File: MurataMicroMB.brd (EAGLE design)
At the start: 90 x 63 mm, 59 parts, among them CON1 C-2395, CON2 WM17143CT-ND, CON3 CON_MIL_10_ARM, CON4 C-2395, IC1 NC7SZ00M5XCT-ND, IC2 296-35164-1-ND, IC3 IC_LPC11U3XQFN33, IC4 AZ1117EH-3.3TRG1DICT-ND, Q1 1253-1168-1-ND, SW1 P-8073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

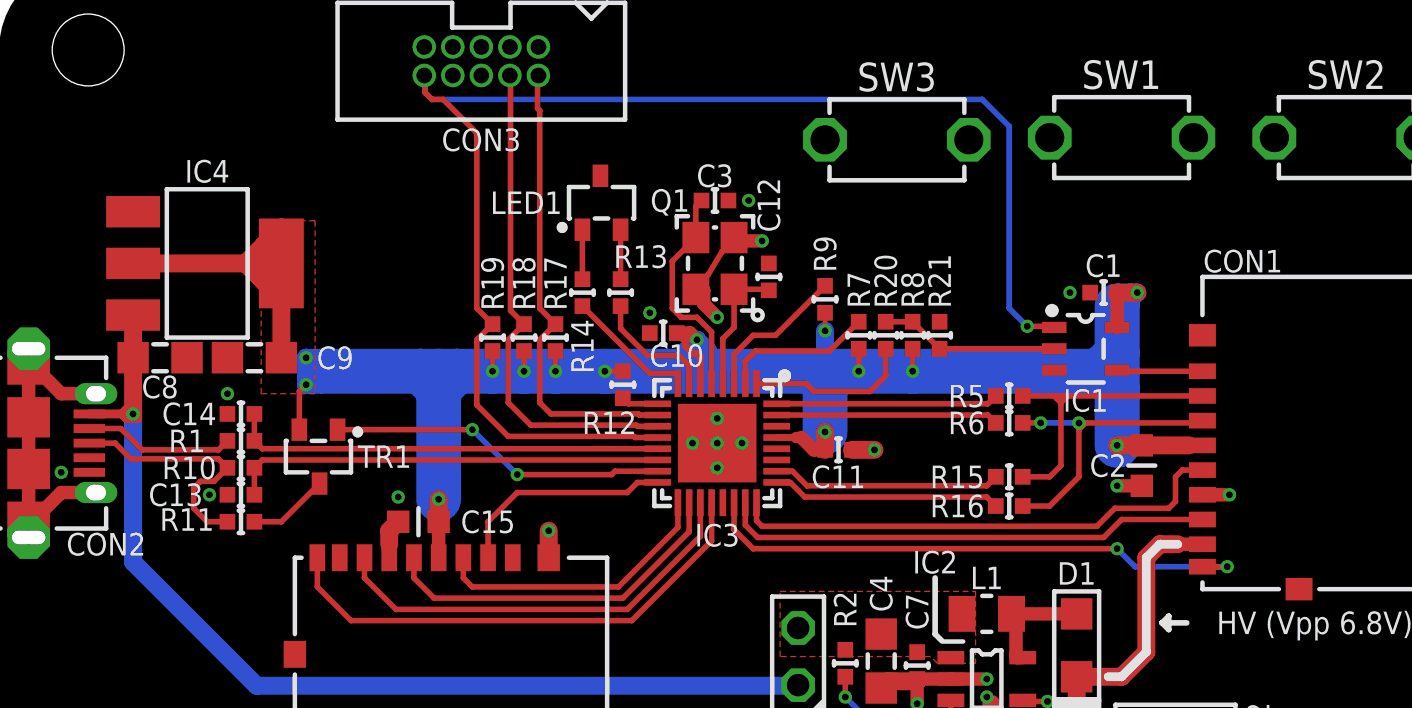
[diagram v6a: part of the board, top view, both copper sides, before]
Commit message: [ MB ] pin1 to be used by TGT_RST; BL=P0_14
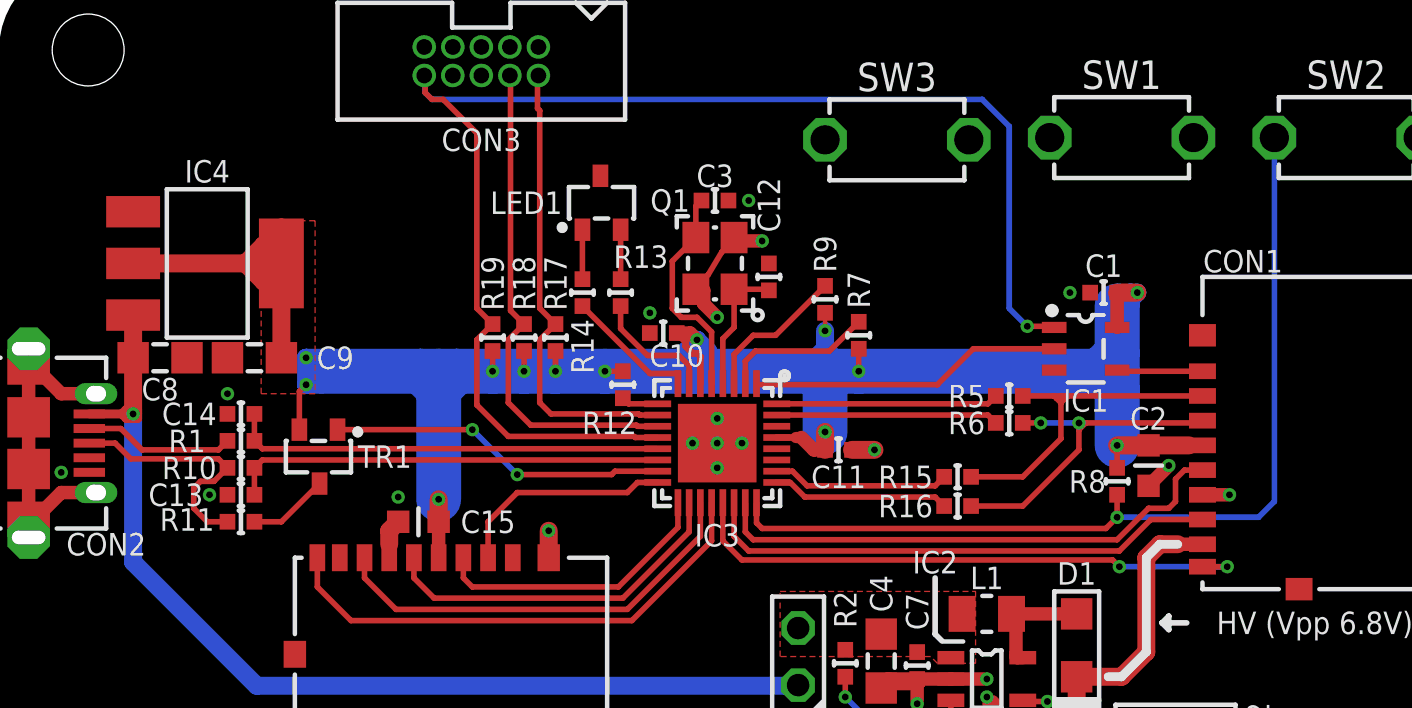
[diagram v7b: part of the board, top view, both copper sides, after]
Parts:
- removed R20, R21: 1k/1005, mylib:C0402
- moved R8 11.2 mm to (59.8, 29.8), turned to 270 degrees
- moved R15 2.30 mm to (52.7, 30.0)
- moved R16 2.30 mm to (52.7, 28.7)
- moved C2 0.30 mm to (61.2, 30.5)
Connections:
- removed net N$19: R21.1, SW2.A2
- removed net N$21: IC3.1, R20.2
- new net TGT_RST: IC1.2, IC3.1
- net BL: now also IC3.24, SW2.A2; no longer IC1.2, R20.1, R21.2
- net DETECT1: now also IC3.21; no longer IC3.22
- net MISO: now also IC3.22; no longer IC3.23
- net SCK: now also IC3.23; no longer IC3.24
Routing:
- net BL: track 8.00 -> 41.8 mm, vias 0 -> 1
- net TGT_RST: track 0.00 -> 13.9 mm
- net N$21: track 7.38 -> 0.00 mm
- net N$18: track 10.2 -> 7.88 mm
- net N$17: track 10.2 -> 7.88 mm
- net 3.3V: track 112.5 -> 114.5 mm, vias 14 -> 13
- net MOSI: track 13.9 -> 15.5 mm
- net !CS!: track 14.3 -> 15.9 mm
- net MISO: track 21.9 -> 23.2 mm
- net SCK: track 22.4 -> 23.7 mm
- net DETECT1: track 24.9 -> 25.7 mm

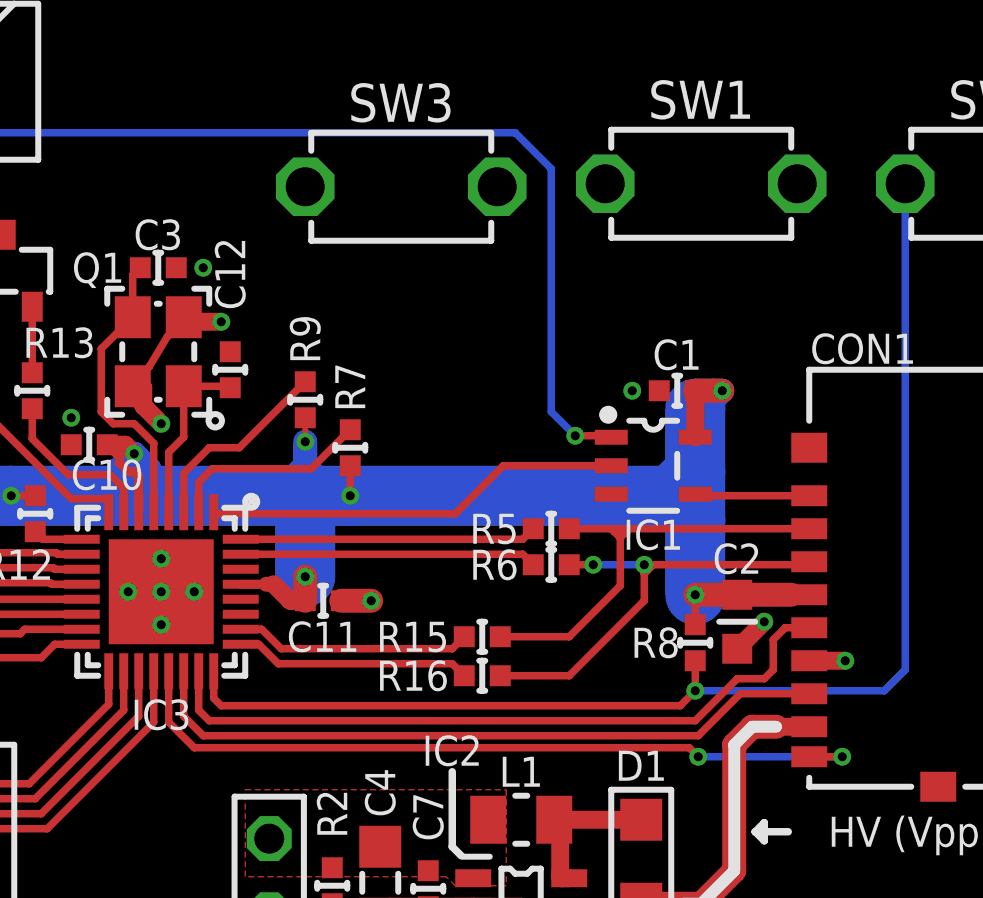
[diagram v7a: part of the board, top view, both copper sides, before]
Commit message: [ MB ] move R7-9/15/16//20,C2,SW1-3; pinout list, library update
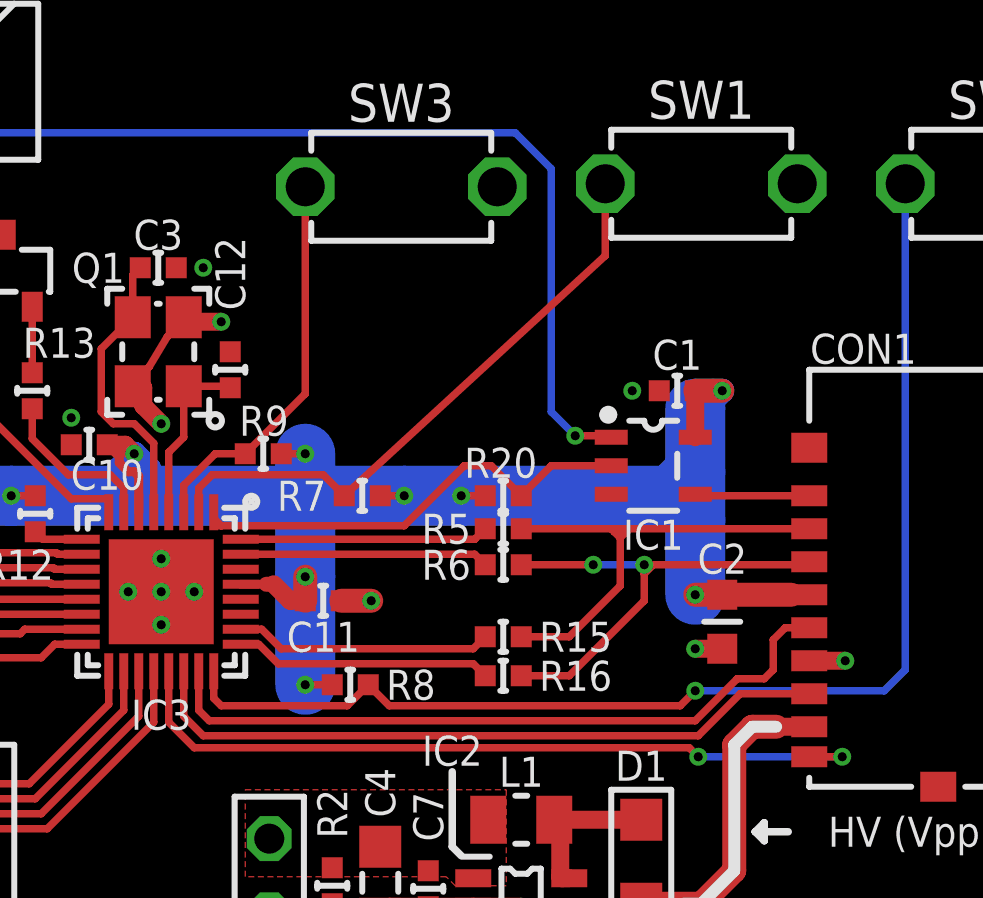
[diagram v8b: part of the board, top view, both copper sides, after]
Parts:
- added R20: 10k/1005, mylib:C0402
- moved R8 11.6 mm to (48.3, 28.4), turned to 0 degrees
- moved R9 2.28 mm to (45.4, 36.1), turned to 180 degrees
- moved R7 1.65 mm to (48.7, 34.7), turned to 180 degrees
- moved R5 1.60 mm to (53.4, 33.6)
- moved R6 1.60 mm to (53.4, 32.4)
- moved R15 0.70 mm to (53.4, 30.0)
- moved R16 0.70 mm to (53.4, 28.7)
- moved C2 0.50 mm to (60.7, 30.5)
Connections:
- net 3.3V: now also R20.1
- net TGT_RST: now also R20.2
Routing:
- net !RESET!: track 6.77 -> 20.3 mm
- net ISP: track 6.61 -> 13.1 mm
- net 3.3V: track 114.5 -> 116.2 mm, vias 13 -> 15
- net N$9: track 9.89 -> 8.29 mm
- net N$6: track 9.89 -> 8.29 mm
- net TGT_RST: track 13.9 -> 15.4 mm
- net MOSI: track 15.5 -> 16.4 mm
- net !CS!: track 15.9 -> 16.8 mm
- net N$18: track 7.88 -> 8.58 mm
- net N$17: track 7.88 -> 8.58 mm
